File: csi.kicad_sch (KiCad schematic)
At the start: 90 parts, among them J701 WE_68715014522, J702 WE_68715014522, Q701 BSS138W-7-F, Q702 BSS138W-7-F, Q703 BSS138W-7-F, Q704 BSS138W-7-F, U701 PCA9547BS, U702 AP22615, U703 AP22615, U704 NX3DV642, U705 NX3DV642, U706 AP22615, U707 AP22615

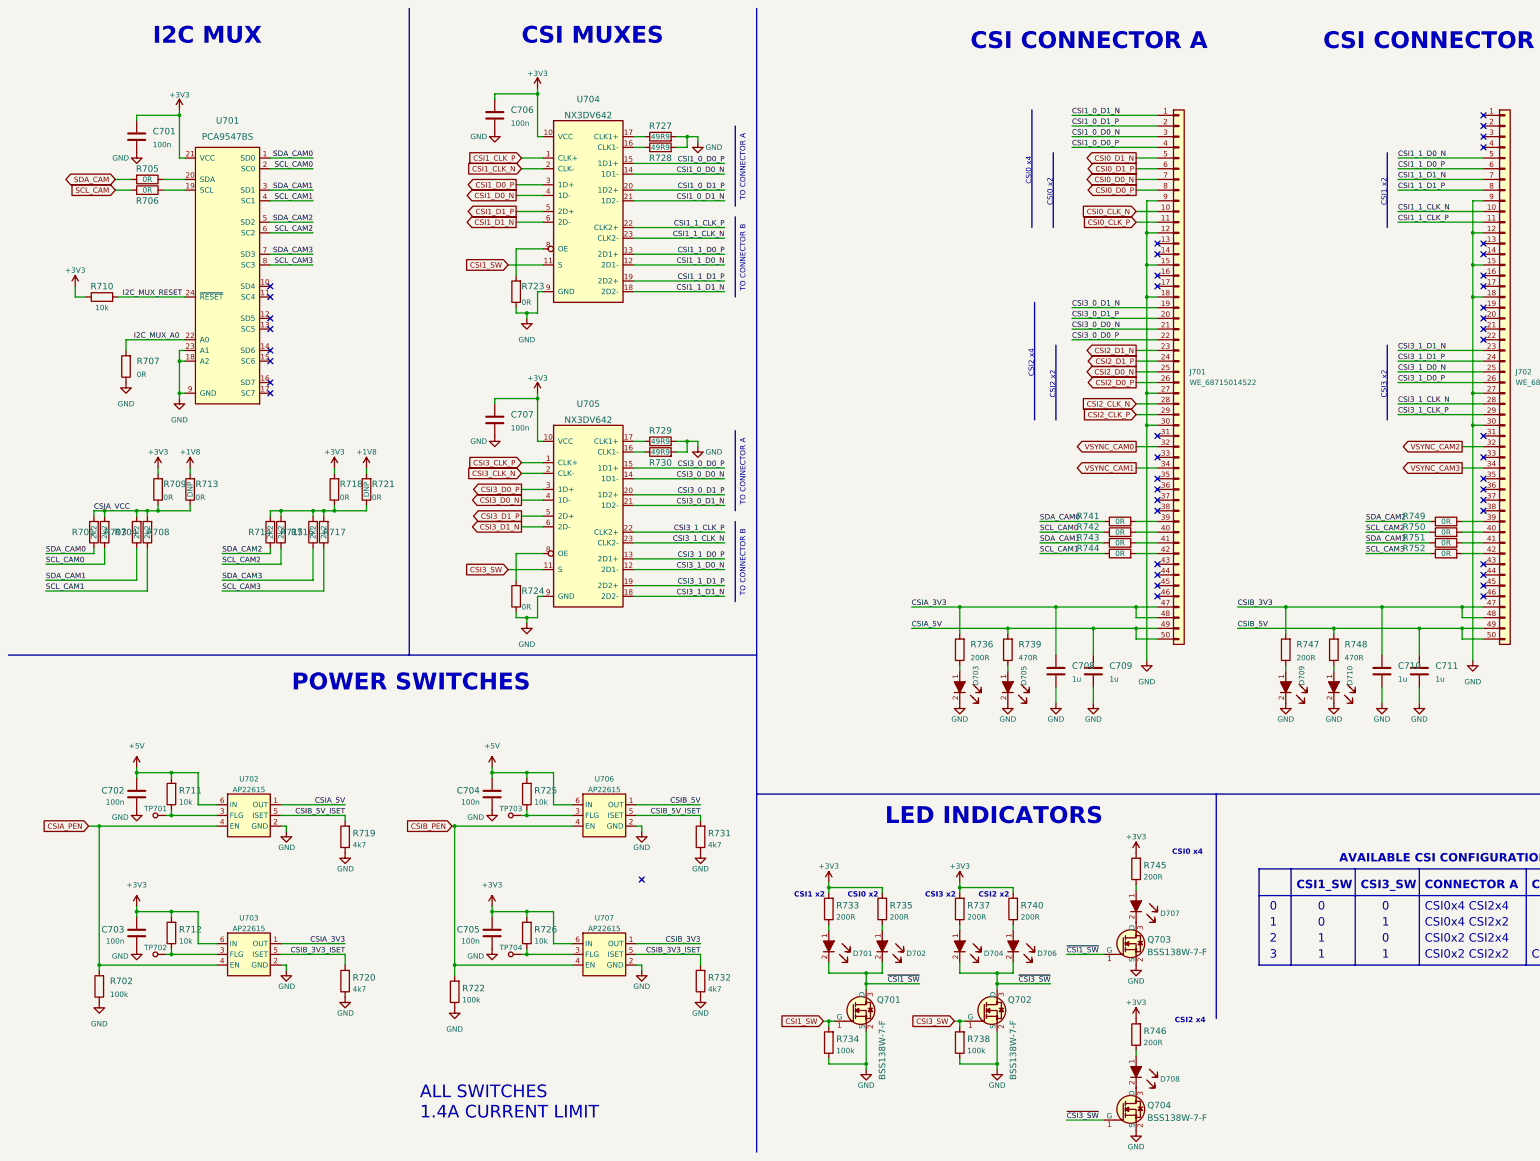
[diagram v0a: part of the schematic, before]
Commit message: Readability improvements
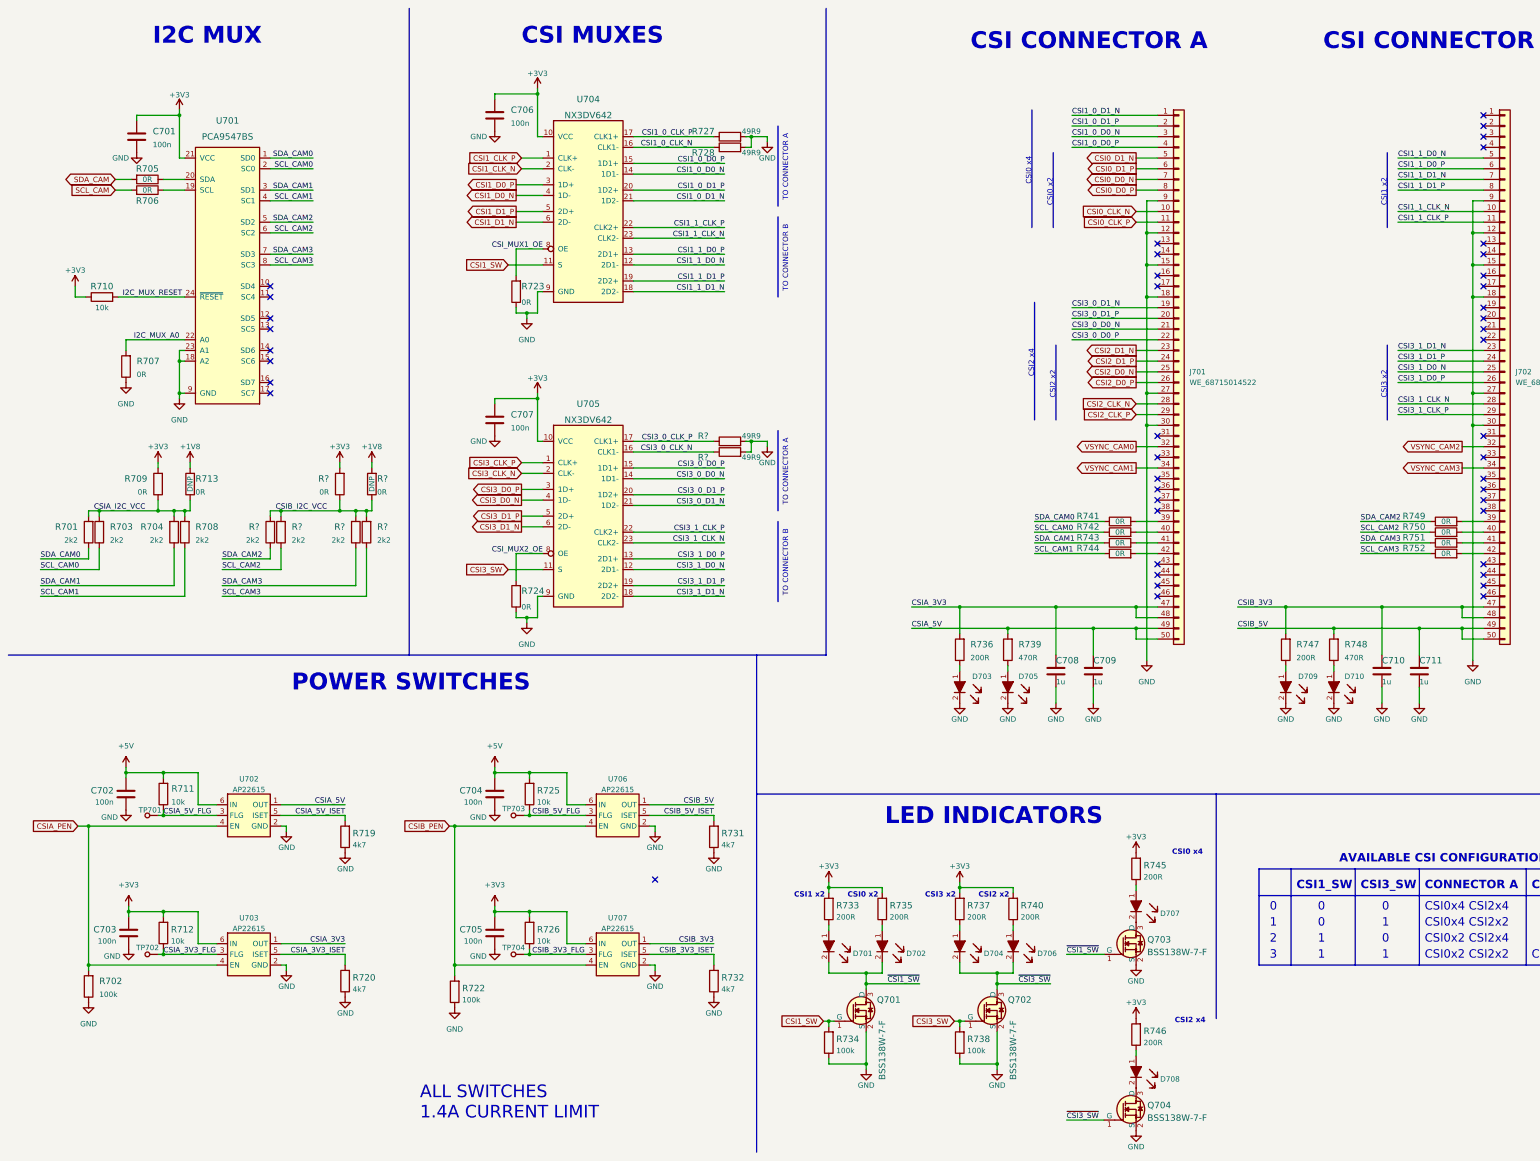
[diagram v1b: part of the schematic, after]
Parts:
- removed R714, R715, R716, R717: R_2k2_0402, antmicro-footprints:0402-res, symbol antmicroResistors0402:R_2k2_0402
- removed R718, R721: R_0R_0402, antmicro-footprints:0402-res, symbol antmicroResistors0402:R_0R_0402
- removed R729, R730: R_49R9_0402, antmicro-footprints:0402-res, symbol antmicroResistors0402:R_49R9_0402
- added R? (x4): R_2k2_0402, antmicro-footprints:0402-res, symbol antmicroResistors0402:R_2k2_0402
- added R? (x2): R_49R9_0402, antmicro-footprints:0402-res, symbol antmicroResistors0402:R_49R9_0402
- added R? (x2): R_0R_0402, antmicro-footprints:0402-res, symbol antmicroResistors0402:R_0R_0402
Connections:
- net +1V8: now also R?.2
- net +3V3: now also R?.2
- net CSIB_3V3_ISET: no longer R720.2, U703.5 (ISET)
- net CSIB_5V_ISET: no longer R719.2, U702.5 (ISET)
- net GND: now also R?.2, R?.2
- net SCL_CAM2: now also R?.1
- net SCL_CAM3: now also R?.1
- net SDA_CAM2: now also R?.1
- net SDA_CAM3: now also R?.1
- net CSIA_5V_FLG: now reaches R711.1, TP701.1, U702.3 (FLG)
- net CSIB_3V3_FLG: now reaches R726.1, TP704.1, U707.3 (FLG)
- net CSI3_0_CLK_P: now reaches U705.17 (CLK1+)
- net CSI3_0_CLK_P: now also R?.1
- net CSI1_0_CLK_N: now reaches R728.1, U704.16 (CLK1-)
- net CSIB_5V_FLG: now reaches R725.1, TP703.1, U706.3 (FLG)
- net CSI_MUX2_OE: now reaches R724.2, U705.8 (OE)
- net CSI3_0_CLK_N: now reaches U705.16 (CLK1-)
- net CSI3_0_CLK_N: now also R?.1
- net CSIA_3V3_FLG: now reaches R712.1, TP702.1, U703.3 (FLG)
- net CSI1_0_CLK_P: now reaches R727.1, U704.17 (CLK1+)
- net CSI_MUX1_OE: now reaches R723.2, U704.8 (OE)
- net CSIA_VCC renamed CSIA_I2C_VCC
- new net CSIA_3V3_ISET: R720.2, U703.5 (ISET)
- new net CSIA_5V_ISET: R719.2, U702.5 (ISET)
- new net CSIB_I2C_VCC: R?.1, R?.1, R?.2, R?.2, R?.2, R?.2
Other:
- moved on the sheet: C702, C703, C704, C705, R701, R702, R703, R704, R708, R709, R711, R712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

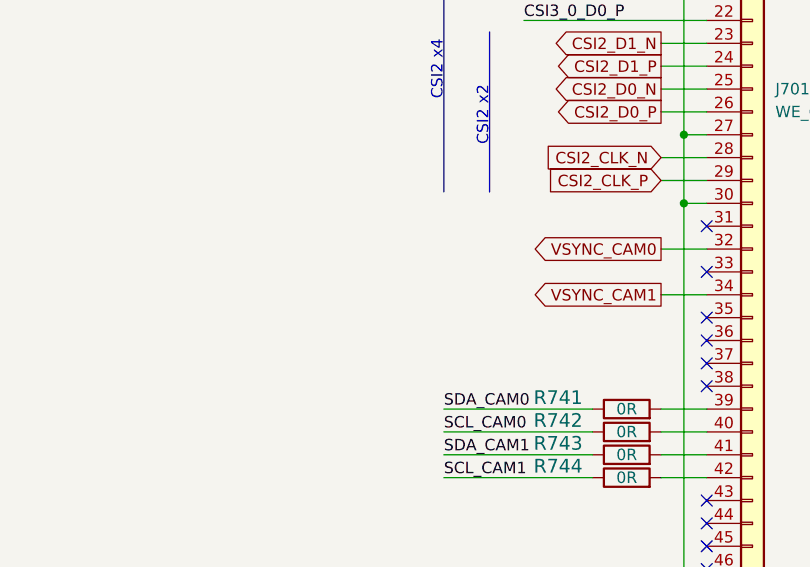
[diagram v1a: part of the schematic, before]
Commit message: Added vsync voltage verification todo note
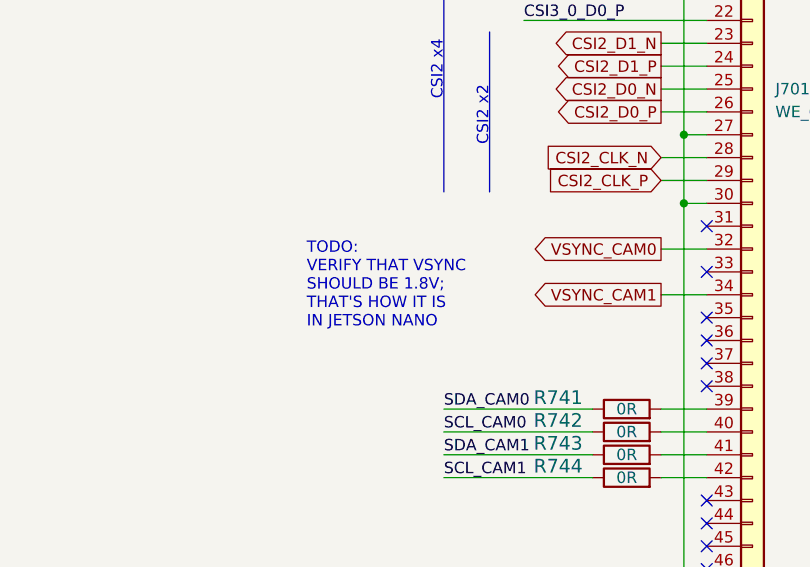
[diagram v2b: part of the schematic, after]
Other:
- note added: "TODO: VERIFY THAT VSYNC SHOULD BE 1.8V; THAT'S HOW IT IS IN JETSON NANO"
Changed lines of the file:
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@@
     (effects (font (size 2 2)) (justify left bottom))
+  )
+  (text "TODO:\nVERIFY THAT VSYNC\nSHOULD BE 1.8V;\nTHAT'S HOW IT IS\nIN JETSON NANO"
+    (at 241.3 125.73 0)
+    (effects (font (size 1.27 1.27)) (justify left bottom))
   )
   (text "CSI3x2" (at 379.73 231.14 0)

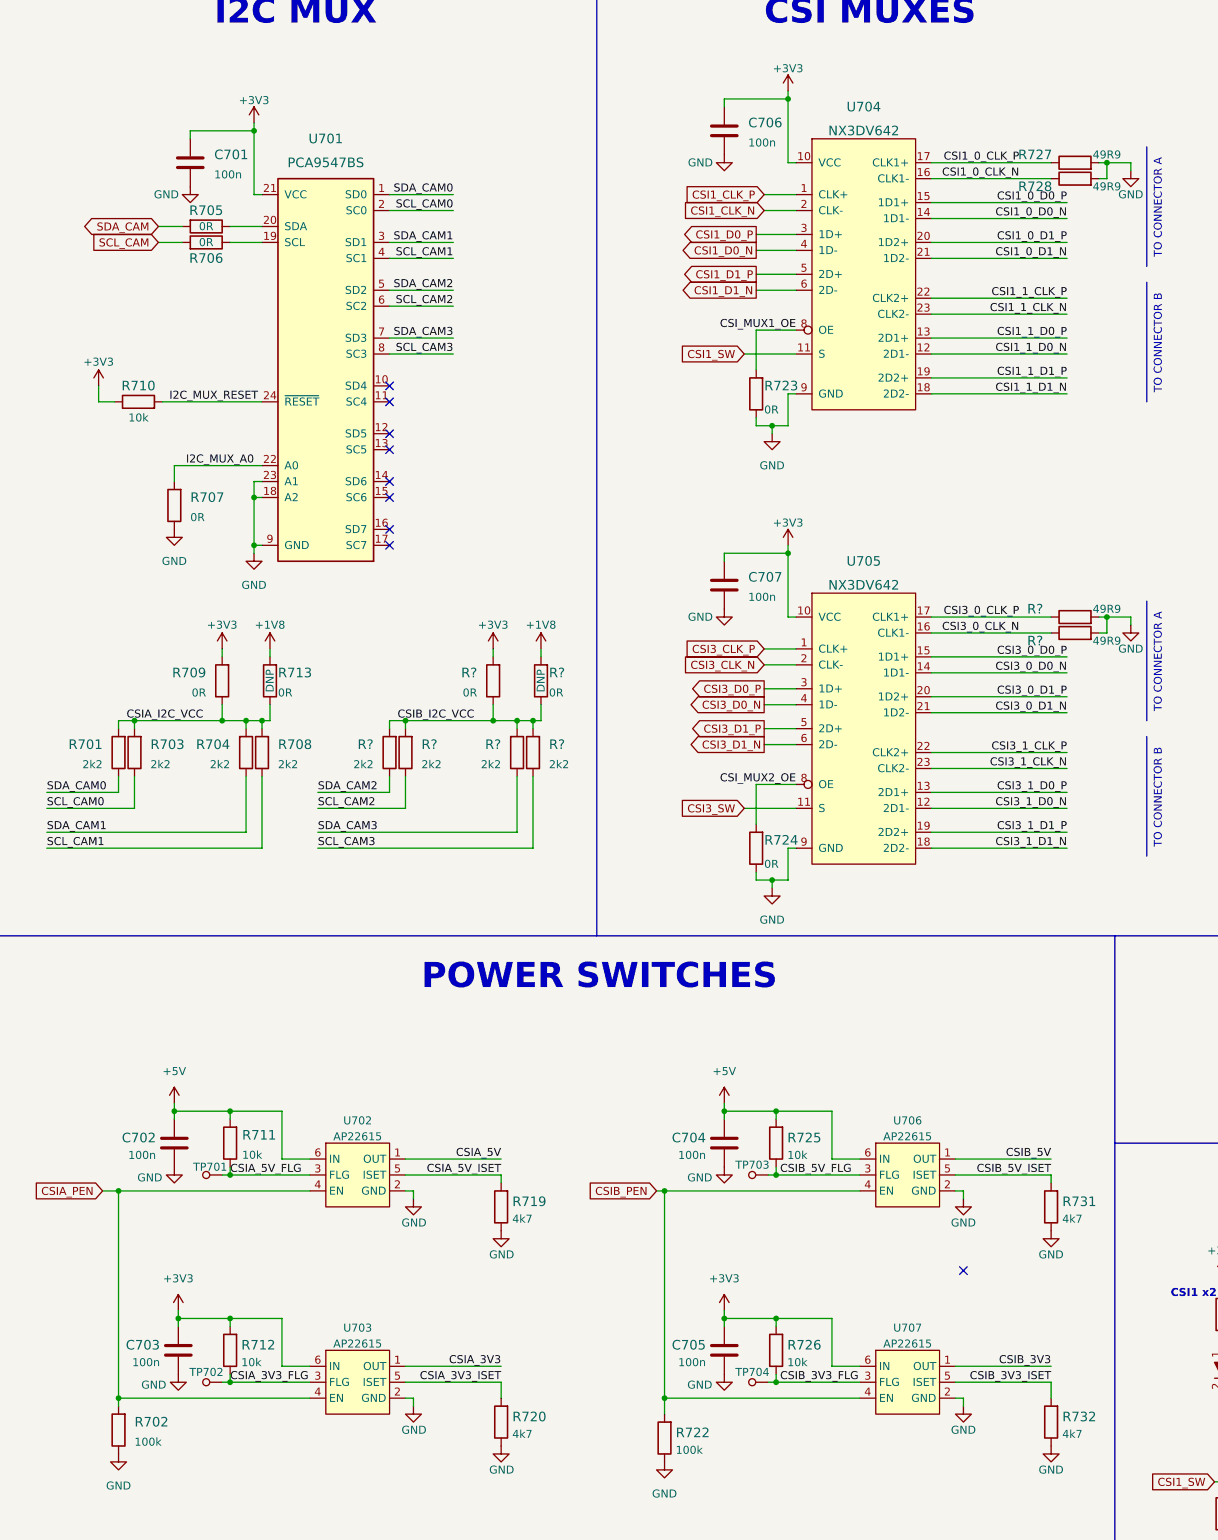
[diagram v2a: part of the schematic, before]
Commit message: Cleaned up the schematic, fixed library issues, annotated schematic
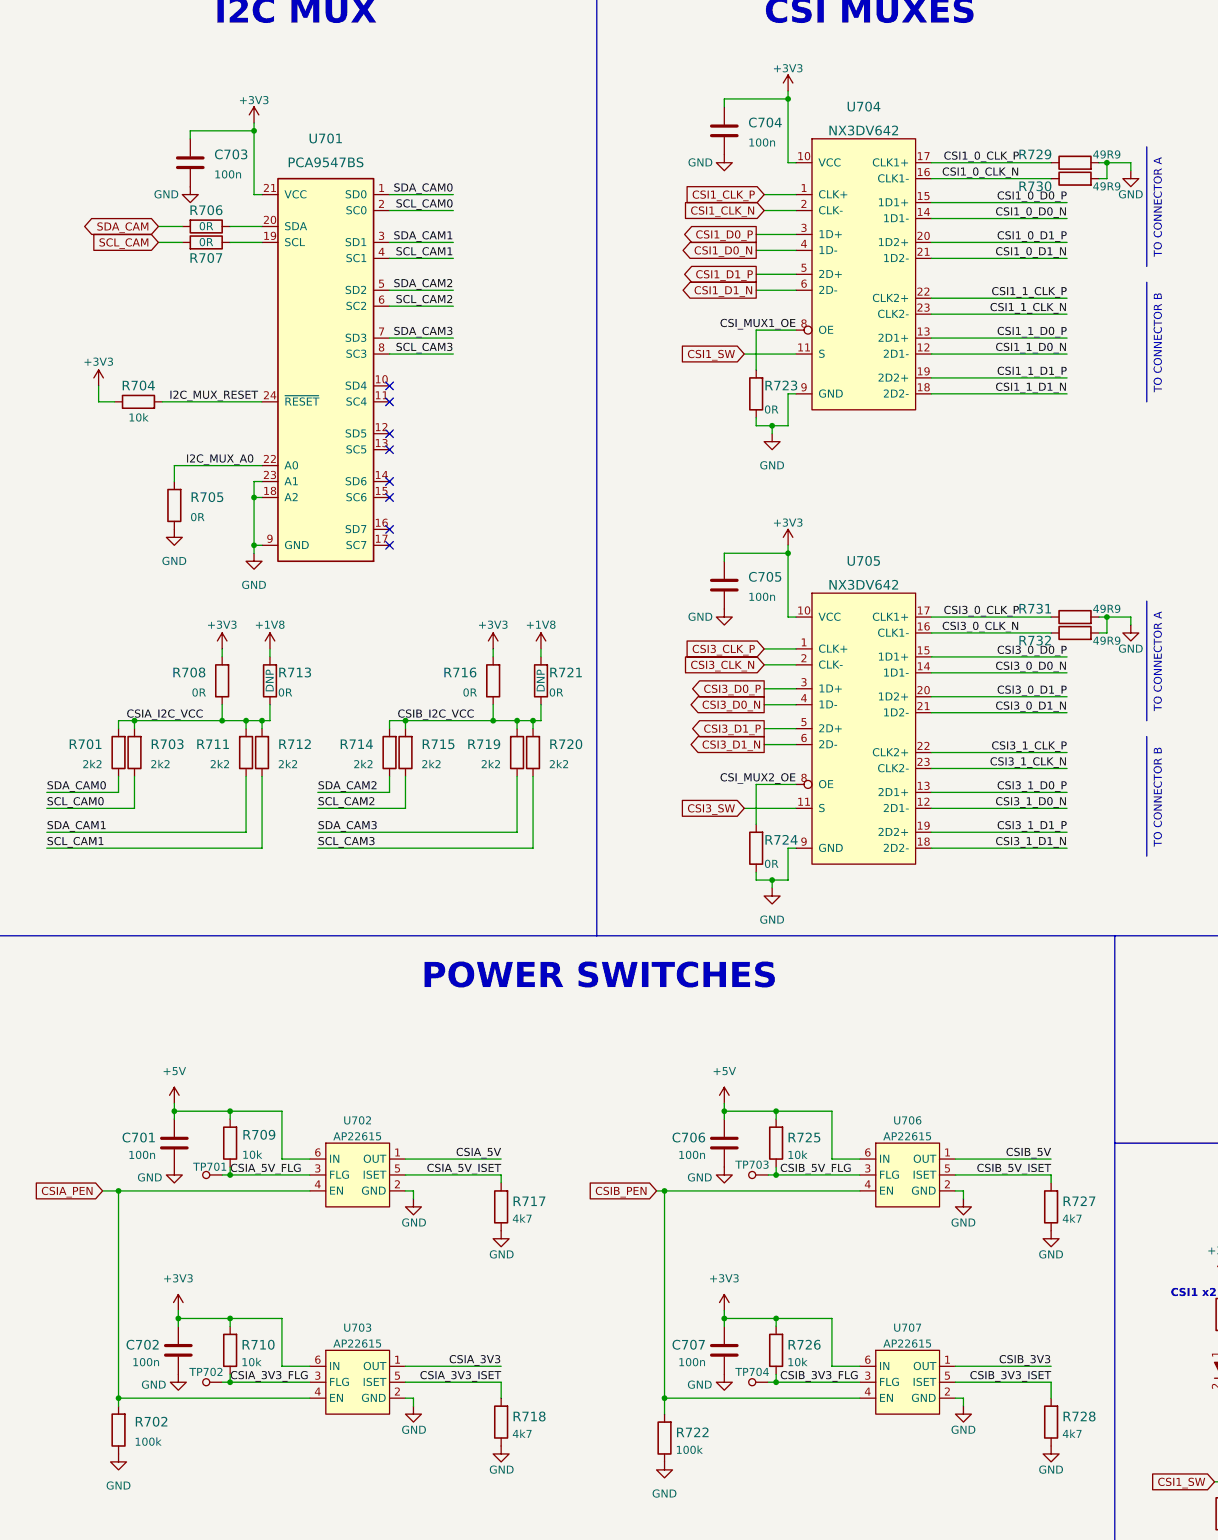
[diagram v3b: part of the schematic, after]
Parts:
- gave numbers to parts that had none: 8
- renumbered C702 to C701, C703 to C702, C701 to C703, C706 to C704, C707 to C705, C704 to C706, C705 to C707, R710 to R704, R707 to R705, R705 to R706, R706 to R707, R709 to R708, R711 to R709, R712 to R710, R704 to R711, R708 to R712, R719 to R717, R720 to R718, R731 to R727, R732 to R728, R727 to R729, R728 to R730
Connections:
- no-connect marks 45 -> 44
